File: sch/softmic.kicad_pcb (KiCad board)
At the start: 2 copper layers, 101.6 x 62.2 mm, 86 parts, among them J1 USB-C Connector, J2 XLR-OUT, J3 AudioJack 3.5mm, P1 4V1, P10 VccPad, P2 4V1, P3 4V1, P4 none, P5 none, P6 none, P7 none, P8 4V1, P9 4V1, Q1 MCP1812BT-033, Q10 ESP32-WROOM, Q11 BC847BS-TP, Q2 MMBFJ201, Q3 CH340G, Q4 BSS64AT116, Q5 OPA1671, Q6 OPA1671, Q7 BQ21040, Q8 MAX11613, Q9 Oled_128_32, SW1 RST, Y1 12MHz

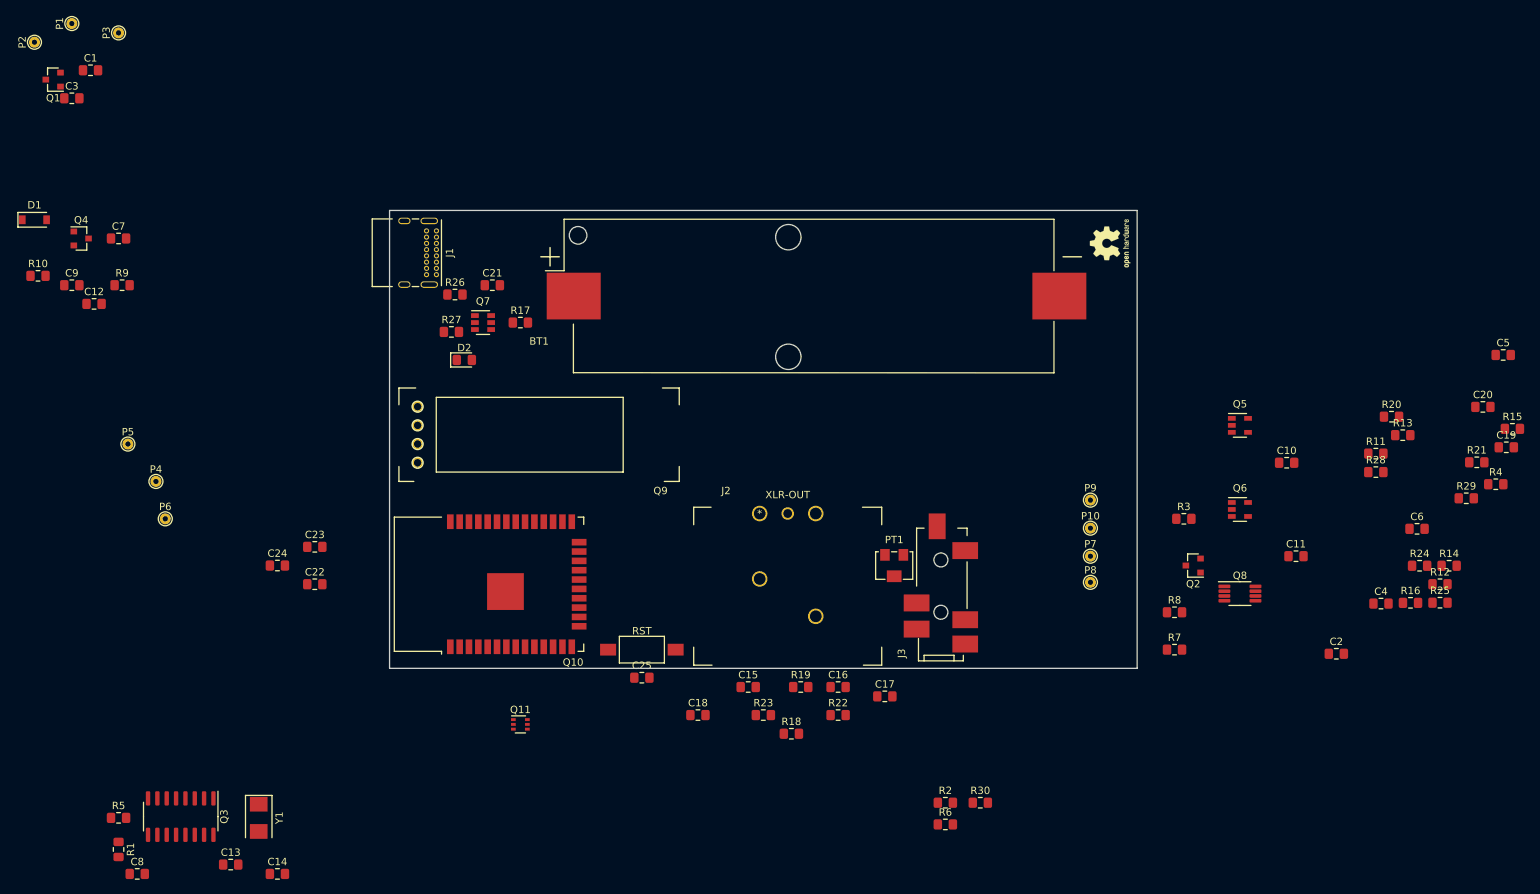
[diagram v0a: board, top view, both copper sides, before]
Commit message: pcb components placed
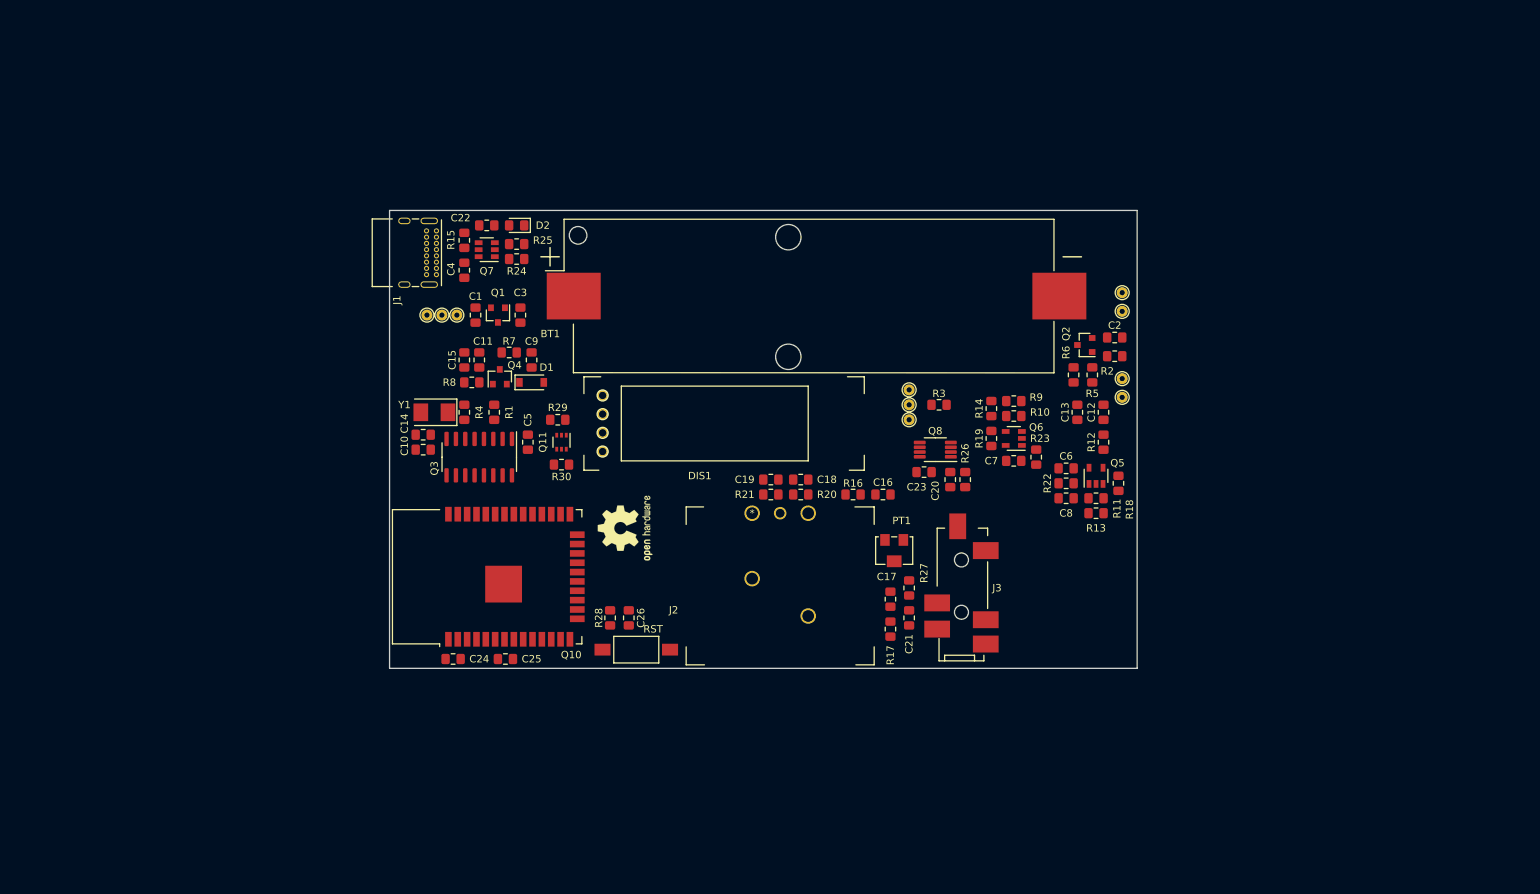
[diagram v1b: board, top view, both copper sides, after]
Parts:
- removed the C19 at (240.7, 90.6)
- removed Q9: Oled_128_32, footprint:OLED-0.91-128x32
- added C20: 5.1n, Capacitor_SMD:C_0805_2012Metric_Pad1.15x1.40mm_HandSolder, F.Cu at (165.1, 95.0)
- added C4: 1u, Capacitor_SMD:C_0805_2012Metric_Pad1.15x1.40mm_HandSolder, F.Cu at (99.1, 66.5)
- added DIS1: Oled_128_32, footprint:OLED-0.91-128x32, F.Cu at (145.8, 92.5)
- logo1: footprint Symbol:OSHW-Logo2_7.3x6mm_SilkScreen -> Symbol:OSHW-Logo2_9.8x8mm_SilkScreen
- moved R5 145.4 mm to (184.4, 80.8), turned to 270 degrees
- moved R15 144.7 mm to (99.1, 62.5), turned to 90 degrees
- moved R4 140.5 mm to (99.1, 85.9), turned to 270 degrees
- moved P5 136.3 mm to (188.5, 72.1), turned to 90 degrees
- moved R25 134.6 mm to (106.2, 63.0), turned to 180 degrees
- moved C13 134.4 mm to (182.4, 85.9), turned to 90 degrees
- moved R10 134.0 mm to (173.7, 86.4)
- moved P6 133.6 mm to (188.5, 69.6), turned to 90 degrees
- moved C8 133.5 mm to (180.8, 97.5)
- moved P4 132.1 mm to (188.5, 81.3), turned to 90 degrees
- moved R24 129.6 mm to (106.2, 65.0), turned to 180 degrees
- moved R29 123.9 mm to (111.8, 86.9)
- moved R9 122.2 mm to (173.7, 84.3), turned to 180 degrees
- moved C5 118.0 mm to (107.7, 89.9), turned to 270 degrees
- moved C11 110.6 mm to (101.1, 78.7), turned to 90 degrees
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- renumbered C9 to C10, C10 to C11, C11 to C12, C12 to C13, C13 to C14, C14 to C15, C15 to C16, C16 to C17, C17 to C18, C18 to C19, C20 to C21, C21 to C22, C22 to C23, C23 to C24, C24 to C25, C25 to C26, C4 to C5, C5 to C6, C6 to C7, C7 to C8, C8 to C9

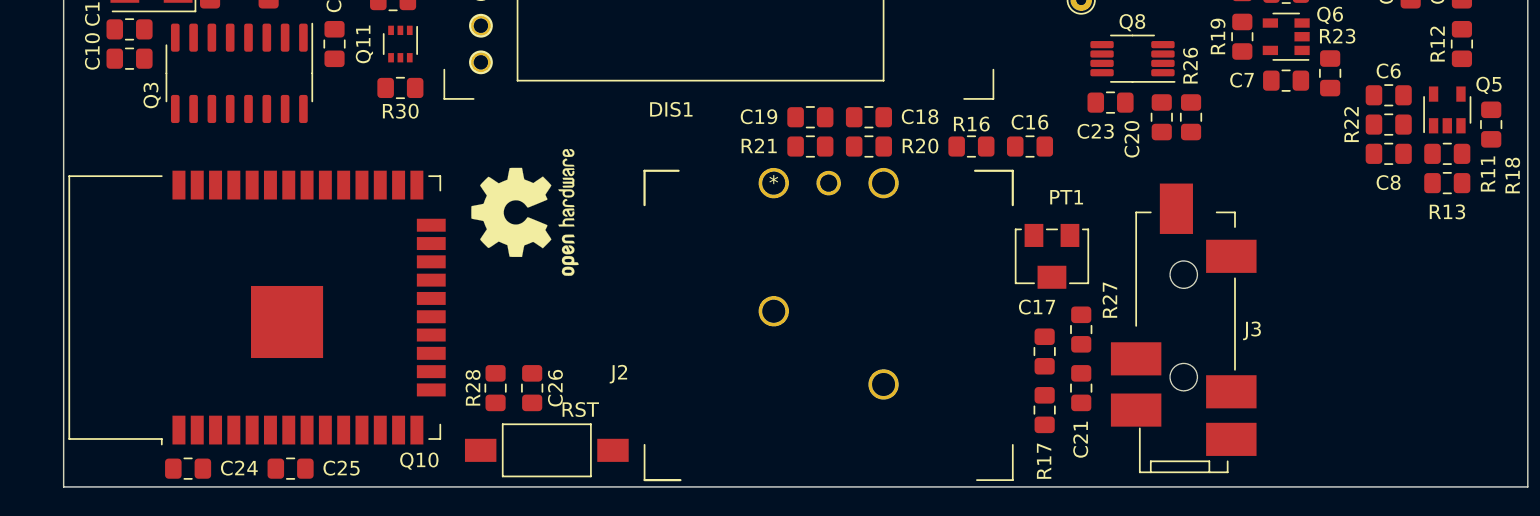
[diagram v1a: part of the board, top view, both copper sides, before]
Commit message: changed ESP32 module for the 16MB version
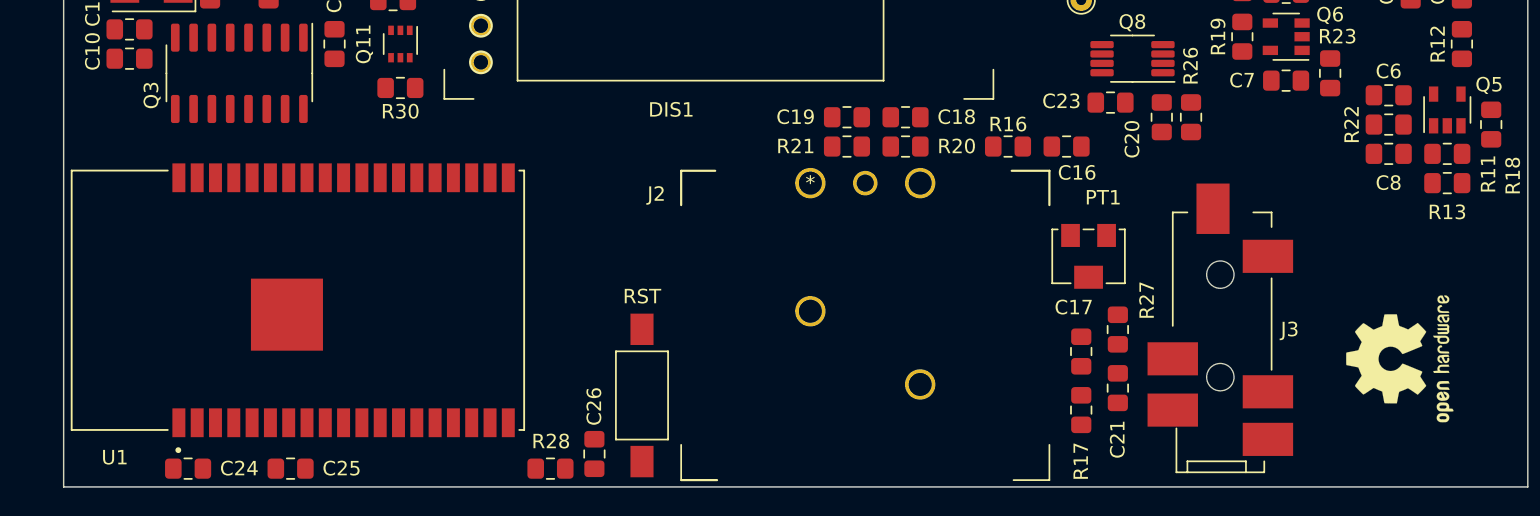
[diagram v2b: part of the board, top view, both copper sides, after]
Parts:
- removed Q10: ESP32-WROOM, RF_Module:ESP32-WROOM-32
- added U1: ESP32-WROVER-B_(16MB), footprint:ESP32-WROVER-B_(16MB), F.Cu at (105.2, 107.7)
- moved logo1 61.6 mm to (181.6, 111.8)
- moved SW1 7.62 mm to (129.0, 114.3), turned to 90 degrees
- moved R28 6.76 mm to (122.7, 119.4), turned to 0 degrees
- moved C26 6.29 mm to (125.7, 118.4)
- moved C16 2.54 mm to (158.5, 97.0)
- moved J2 2.54 mm to (140.7, 99.6)
- moved PT1 2.54 mm to (160.0, 104.6)
- moved C17 2.54 mm to (159.5, 111.3)
- moved C18 2.54 mm to (147.3, 95.0)
- moved C19 2.54 mm to (143.3, 95.0)
- moved C21 2.54 mm to (162.1, 113.8)
- moved J3 2.54 mm to (169.2, 108.0)
- moved R16 2.54 mm to (154.4, 97.0)
- moved R17 2.54 mm to (159.5, 115.3)
- moved R20 2.54 mm to (147.3, 97.0)
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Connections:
- DIS1 pad 1: /I2C_SDA -> Net-(DIS1-Pad1)
- DIS1 pad 2: /I2C_SCL -> Net-(DIS1-Pad2)
